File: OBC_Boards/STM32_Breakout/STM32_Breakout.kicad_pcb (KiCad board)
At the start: 4 copper layers, 95 x 95 mm, 113 parts, among them J1 Conn_02x20_Odd_Even, J2 1050171001, J3 1050171001, J4 105017-1001, J5 SSQ-105-03-T-D, J6 SSQ-105-03-T-D, J7 ST1W008S4ER1500-MicroSDConnec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, J8 105017-1001, Q1 Q_PMOS_DGS, U1 MCP7940NT-I_MS, U2 MCP9808, U3 BU33SA5WGWZ-E2-qsat-symb, U4 STM32L4A6ZGT6P, U5 FSM6JSMATR, U6 MR25H10MDF, U7 FT231XS-R

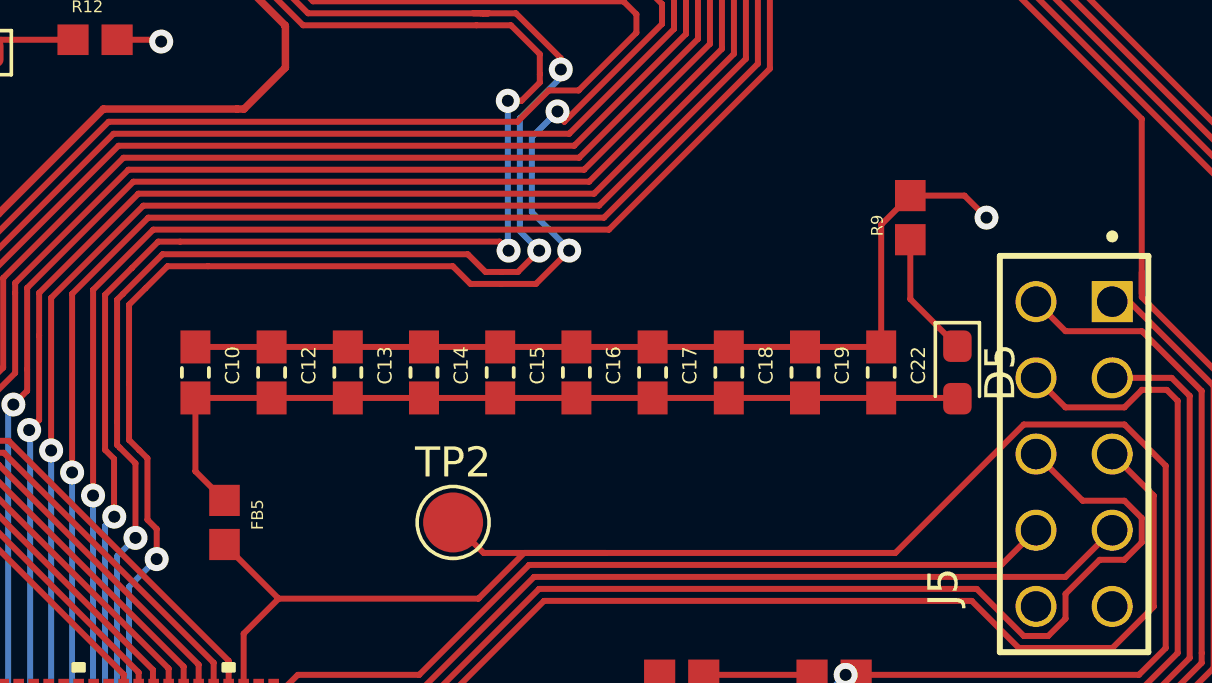
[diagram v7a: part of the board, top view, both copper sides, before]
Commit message: Update capacitors in microcontroller block
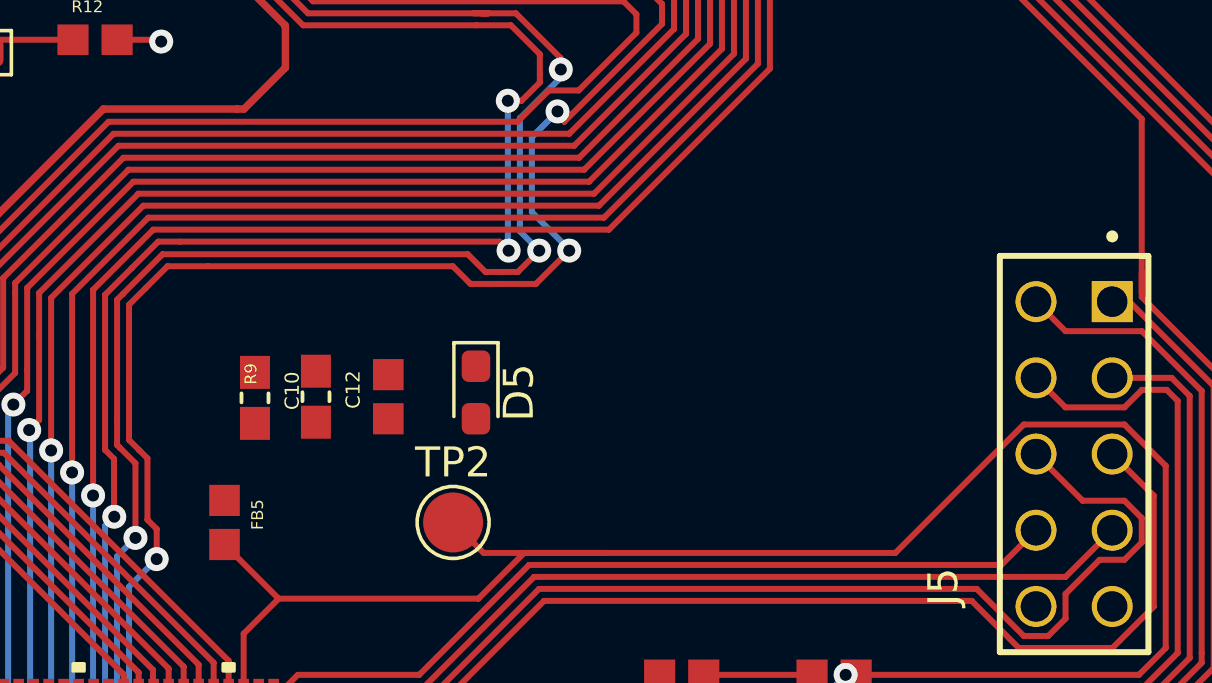
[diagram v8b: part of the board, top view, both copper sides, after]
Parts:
- removed C13, C14, C15, C16, C17, C18, C19, C22: 100n, CAPC1608X90
- C10: footprint CAPC1608X90 -> STM32_Breakout:CAPC1608X90
- C12: value 100n -> 1u; footprint CAPC1608X90 -> STM32_Breakout:CAPC1608X90
- R9: footprint RESC1607X60N -> STM32_Breakout:RESC1607X60N
- moved R9 18.4 mm to (112.1, 77.1)
- moved D5 16.1 mm to (115.1, 76.9)
- moved C10 2.16 mm to (107.7, 77.1)
- moved C12 1.68 mm to (109.7, 77.1)
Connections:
- C10 pad 2: Net-(C10-Pad2) -> VDDMAIN
- C12 pad 2: Net-(C10-Pad2) -> VDDMAIN
- C34 pad 1: Net-(C34-Pad1) -> Net-(C33-Pad2)
- D5 pad 2: Net-(C10-Pad2) -> VDDMAIN
- FB5 pad 1: Net-(C10-Pad2) -> VDDMAIN
- J8 pad 2: Net-(C34-Pad1) -> Net-(J8-Pad2)
- R29 pad 2: Net-(C34-Pad1) -> Net-(J8-Pad2)
- U4 pad 108: +3V3 -> VDDMAIN
- U4 pad 121: +3V3 -> VDDMAIN
- U4 pad 144: +3V3 -> VDDMAIN
- U4 pad 17: +3V3 -> VDDMAIN
- U4 pad 39: +3V3 -> VDDMAIN
- U4 pad 52: +3V3 -> VDDMAIN
- U4 pad 62: +3V3 -> VDDMAIN
- U4 pad 72: +3V3 -> VDDMAIN
- U4 pad 84: +3V3 -> VDDMAIN
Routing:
- net GND: track 171.6 -> 140.5 mm, vias 48 -> 47
- net Net-(C10-Pad2): track 29.2 -> 0.00 mm
- net Net-(J8-Pad2): track 0.00 -> 15.2 mm, vias 0 -> 2
- net Net-(C34-Pad1): track 15.2 -> 0.00 mm, vias 2 -> 0
- net Net-(D5-Pad1): track 4.20 -> 0.00 mm
